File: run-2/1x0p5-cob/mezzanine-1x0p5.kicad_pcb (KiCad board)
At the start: 2 copper layers, 14 x 16 mm, 11 parts

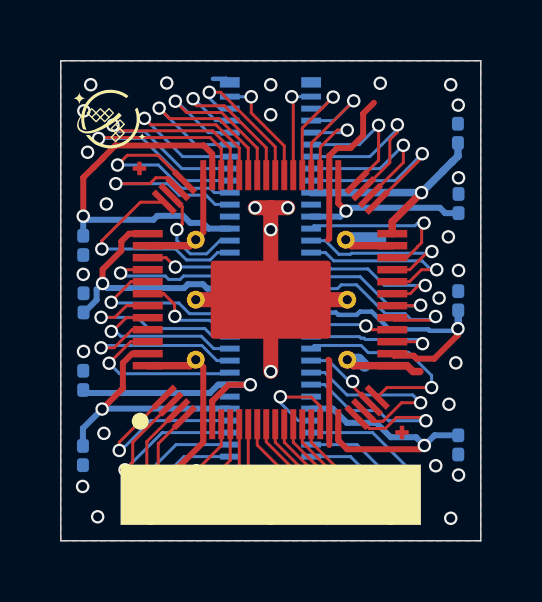
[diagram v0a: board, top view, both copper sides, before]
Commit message: Remove vias from centre of 1x0p5
Switch to 4 layers for 1x0p5
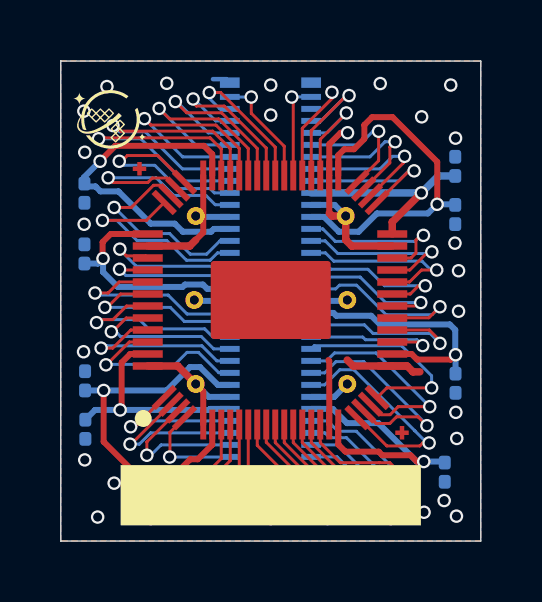
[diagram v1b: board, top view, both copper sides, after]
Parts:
- moved C105 2.75 mm to (147.2, 97.4), turned to -90 degrees
- moved C108 1.74 mm to (134.9, 91.0)
- moved C106 1.63 mm to (134.9, 93.1)
- moved C101 1.10 mm to (147.2, 90.1)
- moved C107 1.02 mm to (146.9, 100.3)
- moved C102 0.88 mm to (134.9, 98.9)
- moved C103 0.38 mm to (147.2, 91.7), turned to -90 degrees
- moved C104 0.06 mm to (134.9, 97.3)
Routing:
- net GND: track 39.2 -> 26.9 mm, vias 32 -> 29
- net VDD_CORE_0: track 6.41 -> 12.3 mm
- net /bidir_13: track 3.53 -> 7.88 mm
- net VDD_CORE_1: track 8.00 -> 12.3 mm
- net /bidir_16: track 2.78 -> 7.04 mm
- net /bidir_19: track 2.78 -> 6.38 mm
- net /bidir_44: track 3.86 -> 7.03 mm
- net /an_3: track 3.55 -> 6.02 mm
- net /an_0: track 2.90 -> 4.99 mm
- net /bidir_0: track 6.62 -> 4.81 mm
- net /bidir_1: track 5.26 -> 3.52 mm
- net /clk: track 6.49 -> 4.91 mm
- net /bidir_10: track 7.59 -> 6.06 mm
- net /rst_n: track 6.84 -> 5.40 mm
- net VDD_IO_2: track 12.7 -> 11.3 mm
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- added copper zone on In1.Cu, net GND
- added copper zone on In2.Cu, net GND
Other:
- copper layers 2 -> 4
- board text added: "wafer.space GF180MCU Run 2"
- board text removed: "wafer.space GF180MCU Run 1"

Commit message: Remove vias from centre of 0p5x1 and 1x1
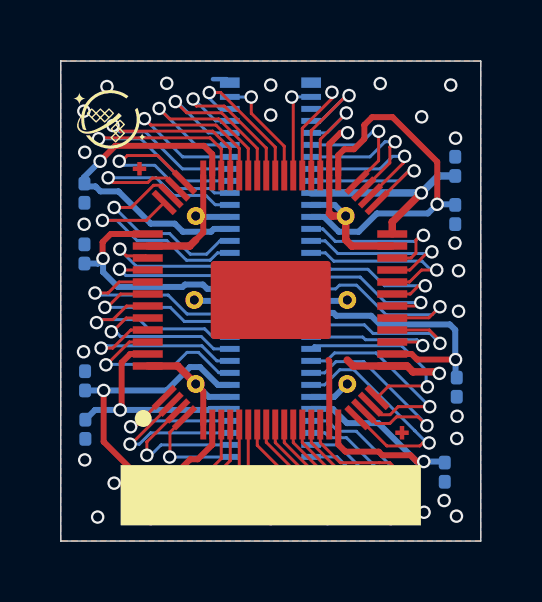
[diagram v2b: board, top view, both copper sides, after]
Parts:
- moved C105 0.14 mm to (147.3, 97.5)
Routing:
- net GND: track 26.9 -> 27.6 mm, vias 29 -> 30
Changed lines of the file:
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@@
 	(footprint "Capacitor_SMD:C_0201_0603Metric"
 		(layer "B.Cu")
-		(at 147.25 97.37 -90)
+		(at 147.29 97.5 -90)
 		(descr "Capacitor SMD 0201 (0603 Metric), square (rectangular) end terminal, IPC_7351 nominal, (Body size source: https://www.vishay.com/docs/20052/crcw0201e3.pdf), generated with kicad-footprint-generator")
 		(tags "capacitor")
@@
 	)
 	(segment
+		(start 143.84 96.794999)
+		(end 143.64 96.594999)
+		(width 0.25)
+		(layer "F.Cu")
+		(net "GND")
+	)
+	(segment
 		(start 138.839999 98.744998)
 		(end 138.839999 97.644998)
@@
 	)
 	(segment
-		(start 143.84 96.794999)
-		(end 143.64 96.594999)
+		(start 143.039998 90.445)
+		(end 143.039998 91.699998)
+		(width 0.2)
+		(layer "F.Cu")
+		(net "GND")
+	)
+	(segment
+		(start 145.83 96.989999)
+		(end 145.634999 96.794999)
 		(width 0.25)
 		(layer "F.Cu")
@@
 	)
 	(segment
-		(start 143.039998 90.445)
-		(end 143.039998 91.699998)
-		(width 0.2)
+		(start 145.634999 96.794999)
+		(end 143.84 96.794999)
+		(width 0.25)
+		(layer "F.Cu")
+		(net "GND")
+	)
+	(segment
+		(start 146.71 97.04)
+		(end 146.659999 96.989999)
+		(width 0.25)
 		(layer "F.Cu")
 		(net "GND")
@@
 	)
 	(segment
-		(start 145.139999 96.794999)
-		(end 143.84 96.794999)
-		(width 0.25)
-		(layer "F.Cu")
-		(net "GND")
-	)
-	(segment
 		(start 136.99 92.794999)
 		(end 138.39 92.794999)
@@
 	)
 	(segment
-		(start 145.139999 96.794999)
-		(end 145.634999 96.794999)
-		(width 0.25)
-		(layer "F.Cu")
-		(net "GND")
-	)
-	(segment
 		(start 137.990001 96.795)
 		(end 138.589999 97.394998)
@@
 	)
 	(segment
-		(start 145.83 96.989999)
-		(end 146.06 96.989999)
+		(start 146.659999 96.989999)
+		(end 145.83 96.989999)
 		(width 0.25)
 		(layer "F.Cu")
@@
 	)
 	(segment
-		(start 145.634999 96.794999)
-		(end 145.83 96.989999)
-		(width 0.25)
-		(layer "F.Cu")
-		(net "GND")
-	)
-	(segment
 		(start 143.134998 91.794998)
 		(end 143.04 91.7)
@@
 	)
 	(via
+		(at 146.71 97.04)
+		(size 0.45)
+		(drill 0.3)
+		(layers "F.Cu" "B.Cu")
+		(net "GND")
+	)
+	(via
 		(at 134.86 88.299999)
 		(size 0.45)
@@
 	)
 	(via
-		(at 147.26 98.34)
+		(at 147.3 98.47)
 		(size 0.45)
 		(drill 0.3)
@@
 	)
 	(segment
-		(start 144.960723 97.524276)
+		(start 146.26 97.46)
+		(end 145.024997 97.46)
+		(width 0.1)
+		(layer "F.Cu")
+		(net "/bidir_17")
+	)
+	(segment
+		(start 146.31 97.49)
+		(end 146.29 97.49)
+		(width 0.1)
+		(layer "F.Cu")
+		(net "/bidir_17")
+	)
+	(segment
+		(start 145.024997 97.46)
 		(end 144.639999 97.844998)
 		(width 0.1)
@@
 	)
 	(segment
-		(start 146.452252 97.524275)
-		(end 144.960723 97.524276)
+		(start 146.29 97.49)
+		(end 146.26 97.46)
 		(width 0.1)
 		(layer "F.Cu")
@@
 	)
 	(via
-		(at 146.452252 97.524275)
+		(at 146.31 97.49)
 		(size 0.45)
 		(drill 0.3)
@@
 	)
 	(segment
-		(start 145.450001 96.12)
-		(end 142.54 96.12)
+		(start 142.54 96.12)
+		(end 142.435 96.225)
 		(width 0.1)
 		(layer "B.Cu")
@@
 	)
 	(segment
-		(start 146.452252 97.524275)
-		(end 146.452252 97.122251)
+		(start 146.31 97.49)
+		(end 146.27 97.45)
 		(width 0.1)
 		(layer "B.Cu")
@@
 	)
 	(segment
-		(start 142.54 96.12)
-		(end 142.435 96.225)
+		(start 145.450001 96.12)
+		(end 142.54 96.12)
 		(width 0.1)
 		(layer "B.Cu")
@@
 	)
 	(segment
-		(start 146.452252 97.122251)
+		(start 146.27 96.939999)
 		(end 145.450001 96.12)
 		(width 0.1)
@@
 	)
 	(segment
-		(start 145.969999 96.58)
-		(end 145.784997 96.394998)
-		(width 0.2)
-		(layer "F.Cu")
-		(net "PWR_AUX_0")
+		(start 146.27 97.45)
+		(end 146.27 96.939999)
+		(width 0.1)
+		(layer "B.Cu")
+		(net "/bidir_17")
 	)
 	(segment
-		(start 147.25 96.42)
-		(end 147.09 96.58)
+		(start 145.784997 96.394998)
+		(end 145.139999 96.395)
 		(width 0.2)
 		(layer "F.Cu")
@@
 	)
 	(segment
-		(start 147.09 96.58)
+		(start 147.25 96.58)
 		(end 145.969999 96.58)
 		(width 0.2)
@@
 	)
 	(segment
-		(start 145.784997 96.394998)
-		(end 145.139999 96.395)
+		(start 145.969999 96.58)
+		(end 145.784997 96.394998)
 		(width 0.2)
 		(layer "F.Cu")
@@
 	)
 	(via
-		(at 147.25 96.42)
+		(at 147.25 96.58)
 		(size 0.45)
 		(drill 0.3)
@@
 	)
 	(segment
-		(start 147.24 96.41)
-		(end 147.24 95.59)
+		(start 143.18 95.024998)
+		(end 142.434999 95.024998)
 		(width 0.2)
 		(layer "B.Cu")
@@
 	)
 	(segment
-		(start 147.25 96.42)
-		(end 147.25 96.376)
-		(width 0.15)
+		(start 147.06 95.41)
+		(end 144.73 95.41)
+		(width 0.2)
 		(layer "B.Cu")
 		(net "PWR_AUX_0")
 	)
 	(segment
-		(start 143.275002 95.12)
-		(end 143.18 95.024998)
+		(start 147.25 96.58)
+		(end 147.25 96.42)
 		(width 0.2)
 		(layer "B.Cu")
@@
 	)
 	(segment
-		(start 144.44 95.12)
-		(end 143.275002 95.12)
+		(start 147.25 96.42)
+		(end 147.24 96.41)
 		(width 0.2)
 		(layer "B.Cu")
@@
 	)
 	(segment
-		(start 147.25 96.42)
-		(end 147.25 97.02)
+		(start 147.25 97.02)
+		(end 147.28 97.05)
 		(width 0.2)
 		(layer "B.Cu")
@@
 	)
 	(segment
-		(start 147.25 96.42)
-		(end 147.24 96.41)
+		(start 143.275002 95.12)
+		(end 143.18 95.024998)
 		(width 0.2)
 		(layer "B.Cu")
@@
 	)
 	(segment
-		(start 147.25 96.376)
-		(end 147.318 96.308)
-		(width 0.15)
+		(start 147.25 96.58)
+		(end 147.25 97.02)
+		(width 0.2)
 		(layer "B.Cu")
 		(net "PWR_AUX_0")
 	)
 	(segment
-		(start 147.24 95.59)
-		(end 147.06 95.41)
+		(start 144.44 95.12)
+		(end 143.275002 95.12)
 		(width 0.2)
 		(layer "B.Cu")
@@
 	)
 	(segment
-		(start 147.25 97.02)
-		(end 147.28 97.05)
+		(start 147.24 95.59)
+		(end 147.06 95.41)
 		(width 0.2)
 		(layer "B.Cu")
@@
 	)
 	(segment
-		(start 147.06 95.41)
-		(end 144.73 95.41)
-		(width 0.2)
+		(start 147.25 96.58)
+		(end 147.25 96.376)
+		(width 0.15)
 		(layer "B.Cu")
 		(net "PWR_AUX_0")
 	)
 	(segment
-		(start 143.18 95.024998)
-		(end 142.434999 95.024998)
+		(start 147.24 96.41)
+		(end 147.24 95.59)
 		(width 0.2)
 		(layer "B.Cu")
@@
 		(polygon
 			(pts
-				(xy 145.91 99.405) (xy 145.059999 99.405) (xy 145.059999 98.48) (xy 145.91 98.479999)
+				(xy 137.61 92.23) (xy 136.34 92.23) (xy 136.34 89.79) (xy 138.78 89.79) (xy 138.78 90.62)
+			)
+		)
+	)
+	(zone
+		(layer "F.Cu")
+		(hatch edge 0.5)
+		(connect_pads
+			(clearance 0)
+		)
+		(min_thickness 0.15)
+		(keepout
+			(tracks allowed)
+			(vias allowed)
+			(pads allowed)
+			(copperpour not_allowed)
+			(footprints allowed)
+		)
+		(placement
+			(enabled no)
+			(sheetname "/")
+		)
+		(fill
+			(thermal_gap 0.5)
+			(thermal_bridge_width 0.5)
+			(island_removal_mode 1)
+		)
+		(polygon
+			(pts
+				(xy 145.91 99.405) (xy 144.52 99.405) (xy 144.52 97.010003) (xy 145.6 97.01) (xy 145.9 97.31)
 			)
 		)
@@
 			)
 		)
+	)
+	(zone
+		(layer "F.Cu")
+		(hatch edge 0.5)
+		(connect_pads
+			(clearance 0)
+		)
+		(min_thickness 0.15)
+		(keepout
+			(tracks allowed)
+			(vias allowed)
+			(pads allowed)
+			(copperpour not_allowed)
+			(footprints allowed)
+		)
+		(placement
+			(enabled no)
+			(sheetname "/")
+		)
+		(fill
+			(thermal_gap 0.5)
+			(thermal_bridge_width 0.5)
+			(island_removal_mode 1)
+		)
+		(polygon
+			(pts
+				(xy 145.77 92.28) (xy 144.69 92.28) (xy 144.379999 91.875001) (xy 144.379999 90.950001) (xy 145.77 90.95)
+			)
+		)
+	)
+	(zone
+		(layer "F.Cu")
+		(hatch edge 0.5)
+		(connect_pads
+			(clearance 0)
+		)
+		(min_thickness 0.15)
+		(keepout
+			(tracks allowed)
+			(vias allowed)
+			(pads allowed)
+			(copperpour not_allowed)
+			(footprints allowed)
+		)
+		(placement
+			(enabled no)
+			(sheetname "/")
+		)
+		(fill
+			(thermal_gap 0.5)
+			(thermal_bridge_width 0.5)
+			(island_removal_mode 1)
+		)
+		(polygon
+			(pts
+				(xy 138.87 98.84) (xy 136.32 98.84) (xy 136.32 96.92) (xy 137.57 96.92)
+			)
+		)

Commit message: Arrow marking, tweak ground flood on 1x1
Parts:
- added G***: LOGO, WaferSpace:ws_top_arrow, F.Cu at (145.1, 90.5)

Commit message: Matching pin 1 through hole on 1x1, 1x0p5, 0p5x1
Remove unneded via annualar rings from 1x0p5 and 0p5x1
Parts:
- added J1: Conn_01x01, WaferSpace:pin1_fiducial, F.Cu at (135.3, 101.4)
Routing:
- net GND: track 27.6 -> 29.7 mm, vias 30 -> 28

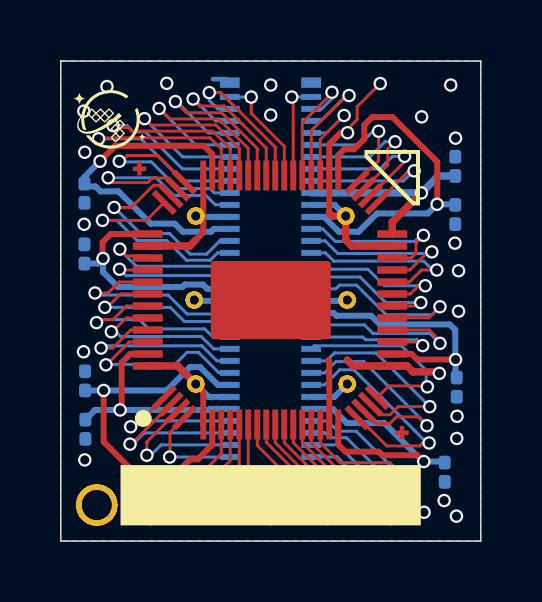
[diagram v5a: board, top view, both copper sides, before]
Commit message: panelize half slots
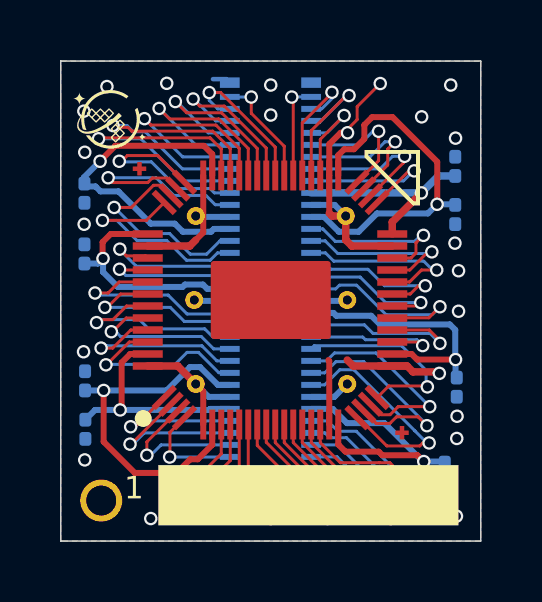
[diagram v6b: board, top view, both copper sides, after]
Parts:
- moved J1 0.21 mm to (135.4, 101.3)
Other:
- board text added: "1"
